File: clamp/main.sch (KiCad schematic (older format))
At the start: 36 parts, among them P1 CONN_01X12, U1 LM741, U2 LM741, U3 LM741, U4 LM741, U5 LM741, U6 LM741

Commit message: change to non hand-soldered 1206
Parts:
- C1, C10, C11, C12, C2, C3, C4, C5, C6, C7, C8, C9: footprint Capacitors_SMD:C_1206_HandSoldering -> Capacitors_SMD:C_1206
- R1, R10, R11, R12, R13, R2, R3, R4, R5, R6, R7, R8, R9: footprint Resistors_SMD:R_1206_HandSoldering -> Resistors_SMD:R_1206
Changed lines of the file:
@@
 F 0 "C3" H 7225 2050 50  0000 L CNN
 F 1 "C" H 7225 1850 50  0000 L CNN
-F 2 "Capacitors_SMD:C_1206_HandSoldering" H 7238 1800 50  0001 C CNN
+F 2 "Capacitors_SMD:C_1206" H 7238 1800 50  0001 C CNN
 F 3 "" H 7200 1950 50  0000 C CNN
 	1    7200 1950
@@
 F 0 "R7" V 5680 1500 50  0000 C CNN
 F 1 "R" V 5600 1500 50  0000 C CNN
-F 2 "Resistors_SMD:R_1206_HandSoldering" V 5530 1500 50  0001 C CNN
+F 2 "Resistors_SMD:R_1206" V 5530 1500 50  0001 C CNN
 F 3 "" H 5600 1500 50  0000 C CNN
 	1    5600 1500
@@
 F 0 "C5" H 7725 2050 50  0000 L CNN
 F 1 "C" H 7725 1850 50  0000 L CNN
-F 2 "Capacitors_SMD:C_1206_HandSoldering" H 7738 1800 50  0001 C CNN
+F 2 "Capacitors_SMD:C_1206" H 7738 1800 50  0001 C CNN
 F 3 "" H 7700 1950 50  0000 C CNN
 	1    7700 1950
@@
 F 0 "R2" V 2930 4000 50  0000 C CNN
 F 1 "R" V 2850 4000 50  0000 C CNN
-F 2 "Resistors_SMD:R_1206_HandSoldering" V 2780 4000 50  0001 C CNN
+F 2 "Resistors_SMD:R_1206" V 2780 4000 50  0001 C CNN
 F 3 "" H 2850 4000 50  0000 C CNN
 	1    2850 4000
@@
 F 0 "R1" V 2380 3450 50  0000 C CNN
 F 1 "R" V 2300 3450 50  0000 C CNN
-F 2 "Resistors_SMD:R_1206_HandSoldering" V 2230 3450 50  0001 C CNN
+F 2 "Resistors_SMD:R_1206" V 2230 3450 50  0001 C CNN
 F 3 "" H 2300 3450 50  0000 C CNN
 	1    2300 3450
@@
 F 0 "R3" V 3980 2050 50  0000 C CNN
 F 1 "R" V 3900 2050 50  0000 C CNN
-F 2 "Resistors_SMD:R_1206_HandSoldering" V 3830 2050 50  0001 C CNN
+F 2 "Resistors_SMD:R_1206" V 3830 2050 50  0001 C CNN
 F 3 "" H 3900 2050 50  0000 C CNN
 	1    3900 2050
@@
 F 0 "R4" V 3980 2250 50  0000 C CNN
 F 1 "R" V 3900 2250 50  0000 C CNN
-F 2 "Resistors_SMD:R_1206_HandSoldering" V 3830 2250 50  0001 C CNN
+F 2 "Resistors_SMD:R_1206" V 3830 2250 50  0001 C CNN
 F 3 "" H 3900 2250 50  0000 C CNN
 	1    3900 2250
@@
 F 0 "R6" V 4030 3350 50  0000 C CNN
 F 1 "R" V 3950 3350 50  0000 C CNN
-F 2 "Resistors_SMD:R_1206_HandSoldering" V 3880 3350 50  0001 C CNN
+F 2 "Resistors_SMD:R_1206" V 3880 3350 50  0001 C CNN
 F 3 "" H 3950 3350 50  0000 C CNN
 	1    3950 3350
@@
 F 0 "R5" V 4030 3100 50  0000 C CNN
 F 1 "R" V 3950 3100 50  0000 C CNN
-F 2 "Resistors_SMD:R_1206_HandSoldering" V 3880 3100 50  0001 C CNN
+F 2 "Resistors_SMD:R_1206" V 3880 3100 50  0001 C CNN
 F 3 "" H 3950 3100 50  0000 C CNN
 	1    3950 3100
@@
 F 0 "C2" H 7475 2050 50  0000 L CNN
 F 1 "C" H 7475 1850 50  0000 L CNN
-F 2 "Capacitors_SMD:C_1206_HandSoldering" H 7488 1800 50  0001 C CNN
+F 2 "Capacitors_SMD:C_1206" H 7488 1800 50  0001 C CNN
 F 3 "" H 7450 1950 50  0000 C CNN
 	1    7450 1950
@@
 F 0 "C1" H 7225 3300 50  0000 L CNN
 F 1 "C" H 7225 3100 50  0000 L CNN
-F 2 "Capacitors_SMD:C_1206_HandSoldering" H 7238 3050 50  0001 C CNN
+F 2 "Capacitors_SMD:C_1206" H 7238 3050 50  0001 C CNN
 F 3 "" H 7200 3200 50  0000 C CNN
 	1    7200 3200
@@
 F 0 "C6" H 7725 3300 50  0000 L CNN
 F 1 "C" H 7725 3100 50  0000 L CNN
-F 2 "Capacitors_SMD:C_1206_HandSoldering" H 7738 3050 50  0001 C CNN
+F 2 "Capacitors_SMD:C_1206" H 7738 3050 50  0001 C CNN
 F 3 "" H 7700 3200 50  0000 C CNN
 	1    7700 3200
@@
 F 0 "C4" H 7475 3300 50  0000 L CNN
 F 1 "C" H 7475 3100 50  0000 L CNN
-F 2 "Capacitors_SMD:C_1206_HandSoldering" H 7488 3050 50  0001 C CNN
+F 2 "Capacitors_SMD:C_1206" H 7488 3050 50  0001 C CNN
 F 3 "" H 7450 3200 50  0000 C CNN
 	1    7450 3200
@@
 F 0 "R9" V 2930 6600 50  0000 C CNN
 F 1 "R" V 2850 6600 50  0000 C CNN
-F 2 "Resistors_SMD:R_1206_HandSoldering" V 2780 6600 50  0001 C CNN
+F 2 "Resistors_SMD:R_1206" V 2780 6600 50  0001 C CNN
 F 3 "" H 2850 6600 50  0000 C CNN
 	1    2850 6600
@@
 F 0 "R8" V 2380 6050 50  0000 C CNN
 F 1 "R" V 2300 6050 50  0000 C CNN
-F 2 "Resistors_SMD:R_1206_HandSoldering" V 2230 6050 50  0001 C CNN
+F 2 "Resistors_SMD:R_1206" V 2230 6050 50  0001 C CNN
 F 3 "" H 2300 6050 50  0000 C CNN
 	1    2300 6050
@@
 F 0 "R10" V 3980 4650 50  0000 C CNN
 F 1 "R" V 3900 4650 50  0000 C CNN
-F 2 "Resistors_SMD:R_1206_HandSoldering" V 3830 4650 50  0001 C CNN
+F 2 "Resistors_SMD:R_1206" V 3830 4650 50  0001 C CNN
 F 3 "" H 3900 4650 50  0000 C CNN
 	1    3900 4650
@@
 F 0 "R11" V 3980 4850 50  0000 C CNN
 F 1 "R" V 3900 4850 50  0000 C CNN
-F 2 "Resistors_SMD:R_1206_HandSoldering" V 3830 4850 50  0001 C CNN
+F 2 "Resistors_SMD:R_1206" V 3830 4850 50  0001 C CNN
 F 3 "" H 3900 4850 50  0000 C CNN
 	1    3900 4850
@@
 F 0 "R13" V 4030 5950 50  0000 C CNN
 F 1 "R" V 3950 5950 50  0000 C CNN
-F 2 "Resistors_SMD:R_1206_HandSoldering" V 3880 5950 50  0001 C CNN
+F 2 "Resistors_SMD:R_1206" V 3880 5950 50  0001 C CNN
 F 3 "" H 3950 5950 50  0000 C CNN
 	1    3950 5950
@@
 F 0 "R12" V 4030 5700 50  0000 C CNN
 F 1 "R" V 3950 5700 50  0000 C CNN
-F 2 "Resistors_SMD:R_1206_HandSoldering" V 3880 5700 50  0001 C CNN
+F 2 "Resistors_SMD:R_1206" V 3880 5700 50  0001 C CNN
 F 3 "" H 3950 5700 50  0000 C CNN
 	1    3950 5700
@@
 F 0 "C7" H 7975 2050 50  0000 L CNN
 F 1 "C" H 7975 1850 50  0000 L CNN
-F 2 "Capacitors_SMD:C_1206_HandSoldering" H 7988 1800 50  0001 C CNN
+F 2 "Capacitors_SMD:C_1206" H 7988 1800 50  0001 C CNN
 F 3 "" H 7950 1950 50  0000 C CNN
 	1    7950 1950
@@
 F 0 "C11" H 8475 2050 50  0000 L CNN
 F 1 "C" H 8475 1850 50  0000 L CNN
-F 2 "Capacitors_SMD:C_1206_HandSoldering" H 8488 1800 50  0001 C CNN
+F 2 "Capacitors_SMD:C_1206" H 8488 1800 50  0001 C CNN
 F 3 "" H 8450 1950 50  0000 C CNN
 	1    8450 1950
@@
 F 0 "C9" H 8225 2050 50  0000 L CNN
 F 1 "C" H 8225 1850 50  0000 L CNN
-F 2 "Capacitors_SMD:C_1206_HandSoldering" H 8238 1800 50  0001 C CNN
+F 2 "Capacitors_SMD:C_1206" H 8238 1800 50  0001 C CNN
 F 3 "" H 8200 1950 50  0000 C CNN
 	1    8200 1950
@@
 F 0 "C8" H 7975 3300 50  0000 L CNN
 F 1 "C" H 7975 3100 50  0000 L CNN
-F 2 "Capacitors_SMD:C_1206_HandSoldering" H 7988 3050 50  0001 C CNN
+F 2 "Capacitors_SMD:C_1206" H 7988 3050 50  0001 C CNN
 F 3 "" H 7950 3200 50  0000 C CNN
 	1    7950 3200
@@
 F 0 "C12" H 8475 3300 50  0000 L CNN
 F 1 "C" H 8475 3100 50  0000 L CNN
-F 2 "Capacitors_SMD:C_1206_HandSoldering" H 8488 3050 50  0001 C CNN
+F 2 "Capacitors_SMD:C_1206" H 8488 3050 50  0001 C CNN
 F 3 "" H 8450 3200 50  0000 C CNN
 	1    8450 3200
@@
 F 0 "C10" H 8225 3300 50  0000 L CNN
 F 1 "C" H 8225 3100 50  0000 L CNN
-F 2 "Capacitors_SMD:C_1206_HandSoldering" H 8238 3050 50  0001 C CNN
+F 2 "Capacitors_SMD:C_1206" H 8238 3050 50  0001 C CNN
 F 3 "" H 8200 3200 50  0000 C CNN
 	1    8200 3200

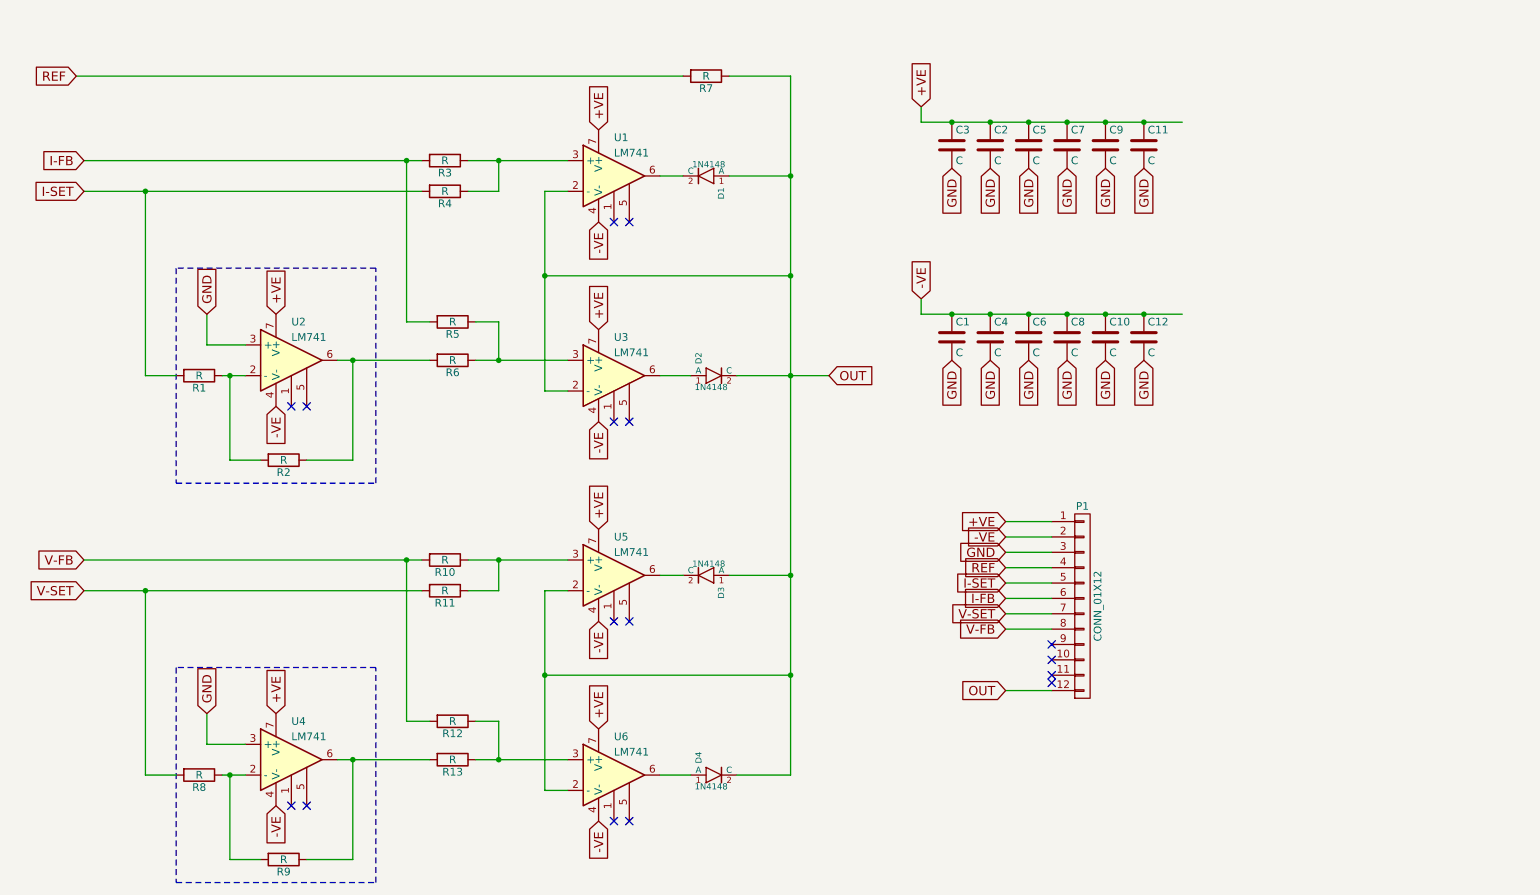
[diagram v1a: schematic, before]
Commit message: add 0R jumpers
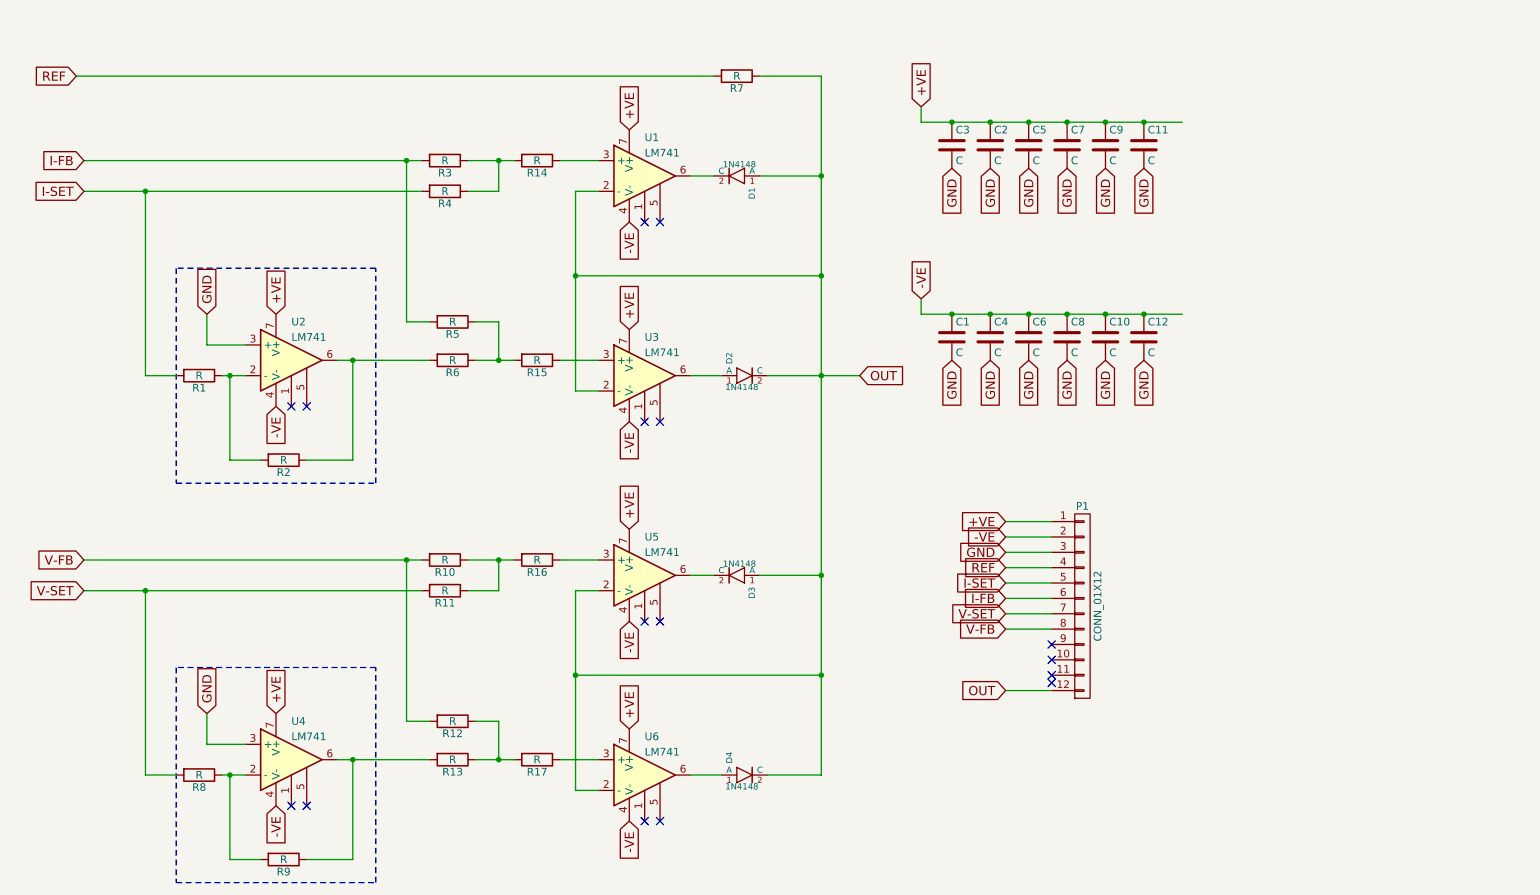
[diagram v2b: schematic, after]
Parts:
- added R14, R15, R16, R17: R, Resistors_SMD:R_1206, symbol R
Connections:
- net at R3.1, R4.1: now also R14.2; no longer U1.3 (+)
- net at R5.1, R6.1: now also R15.2; no longer U3.3 (+)
- net at R10.1, R11.1: now also R16.2; no longer U5.3 (+)
- net at R12.1, R13.1: now also R17.2; no longer U6.3 (+)
- new net: R14.1, U1.3 (+)
- new net: R15.1, U3.3 (+)
- new net: R16.1, U5.3 (+)
- new net: R17.1, U6.3 (+)
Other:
- moved on the sheet: D1, D2, D3, D4, R7, U1, U3, U5, U6

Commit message: add 0R values
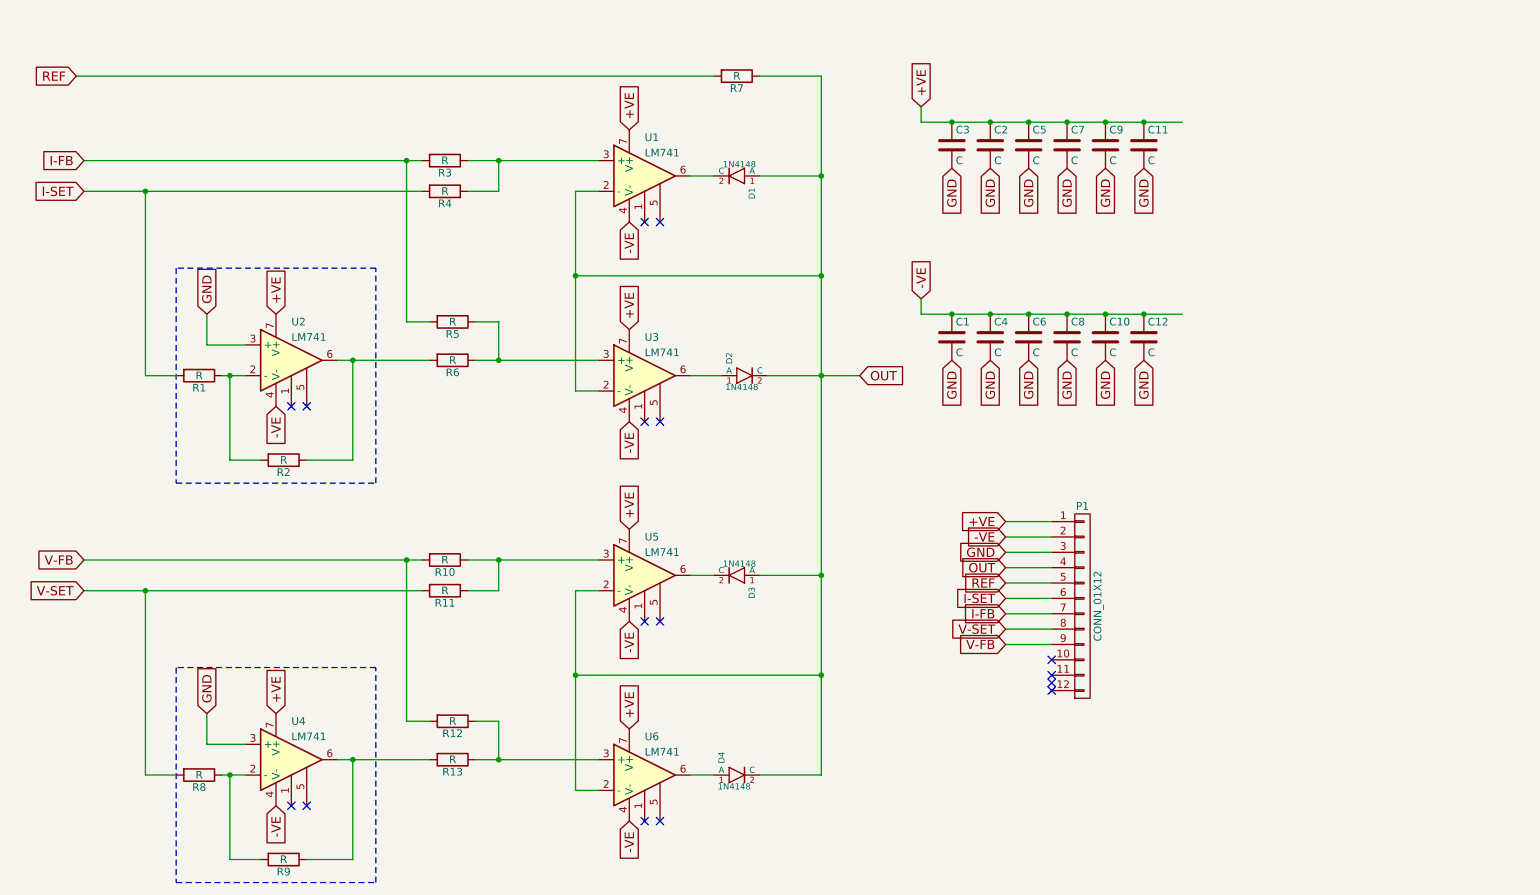
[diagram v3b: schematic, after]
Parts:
- removed R14, R15, R16, R17: R, Resistors_SMD:R_1206, symbol R
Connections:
- net I-FB: now also P1.7 (P7); no longer P1.6 (P6)
- net I-SET: now also P1.6 (P6); no longer P1.5 (P5)
- net OUT: now also P1.4 (P4); no longer P1.12 (P12)
- net REF: now also P1.5 (P5); no longer P1.4 (P4)
- net V-FB: now also P1.9 (P9); no longer P1.8 (P8)
- net V-SET: now also P1.8 (P8); no longer P1.7 (P7)
- net at U1.3 (+): now also R3.1, R4.1
- net at U3.3 (+): now also R5.1, R6.1
- net at U5.3 (+): now also R10.1, R11.1
- net at U6.3 (+): now also R12.1, R13.1
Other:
- moved on the sheet: D4
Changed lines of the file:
@@
 	4750 2250 4900 2250
 Wire Wire Line
-	4050 2050 4350 2050
+	4050 2050 4900 2050
 Wire Wire Line
 	5950 2150 6350 2150
@@
 	4250 3100 4250 3350
 Wire Wire Line
-	4100 3350 4350 3350
+	4100 3350 4900 3350
 Connection ~ 4250 3350
 Wire Notes Line
 	3450 4150 3450 2750
-Text GLabel 7550 4800 0    60   Input ~ 0
+Text GLabel 7550 4900 0    60   Input ~ 0
 I-SET
 Wire Wire Line
@@
 Text GLabel 7550 4600 0    60   Input ~ 0
 GND
-Text GLabel 7550 4700 0    60   Input ~ 0
+Text GLabel 7550 4800 0    60   Input ~ 0
 REF
 Wire Wire Line
@@
 	7850 4700 7550 4700
 Wire Wire Line
-	7850 4800 7550 4800
-Text GLabel 7550 4900 0    60   Input ~ 0
+	7850 4900 7550 4900
+Text GLabel 7550 5000 0    60   Input ~ 0
 I-FB
 Wire Wire Line
-	7850 4900 7550 4900
+	7850 5000 7550 5000
 Connection ~ 6350 3450
 Text GLabel 6600 3450 2    60   Input ~ 0
 OUT
-Text GLabel 7550 5500 0    60   Input ~ 0
+Text GLabel 7550 4700 0    60   Input ~ 0
 OUT
-Wire Wire Line
-	7850 5500 7550 5500
-NoConn ~ 7850 5200
 NoConn ~ 7850 5300
 NoConn ~ 7850 5450
@@
 	4750 4850 4900 4850
 Wire Wire Line
-	4050 4650 4350 4650
+	4050 4650 4900 4650
 Wire Wire Line
 	6350 4750 5950 4750
@@
 L 1N4148 D4
 U 1 1 580862BA
-P 5850 6050
-F 0 "D4" V 5775 6125 40  0000 L BNN
-F 1 "1N4148" H 5725 5975 40  0000 L CNN
-F 2 "Diodes_SMD:MiniMELF_Standard" H 5850 6200 30  0001 C CNN
-F 3 "" H 5850 6050 60  0000 C CNN
-	1    5850 6050
-	1    0    0    -1
-$EndComp
-Wire Wire Line
-	5500 6050 5700 6050
+P 5800 6050
+F 0 "D4" V 5725 6125 40  0000 L BNN
+F 1 "1N4148" H 5675 5975 40  0000 L CNN
+F 2 "Diodes_SMD:MiniMELF_Standard" H 5800 6200 30  0001 C CNN
+F 3 "" H 5800 6050 60  0000 C CNN
+	1    5800 6050
+	1    0    0    -1
+$EndComp
+Wire Wire Line
+	5500 6050 5650 6050
 Connection ~ 6350 5400
 $Comp
@@
 	4250 5700 4250 5950
 Wire Wire Line
-	4100 5950 4350 5950
+	4100 5950 4900 5950
 Connection ~ 4250 5950
 Wire Notes Line
@@
 Text GLabel 1550 4650 0    60   Input ~ 0
 V-FB
+Text GLabel 7550 5200 0    60   Input ~ 0
+V-FB
 Text GLabel 7550 5100 0    60   Input ~ 0
-V-FB
-Text GLabel 7550 5000 0    60   Input ~ 0
 V-SET
 $Comp
@@
 $EndComp
 Wire Wire Line
-	7550 5000 7850 5000
-Wire Wire Line
 	7550 5100 7850 5100
 Wire Wire Line
-	6350 6050 6000 6050
+	6350 6050 5950 6050
 $Comp
 L C C7
@@
 Text GLabel 8450 3350 3    60   Input ~ 0
 GND
-$Comp
-L R R14
-U 1 1 580AC25D
-P 4500 2050
-F 0 "R14" V 4580 2050 50  0000 C CNN
-F 1 "R" V 4500 2050 50  0000 C CNN
-F 2 "Resistors_SMD:R_1206" V 4430 2050 50  0001 C CNN
-F 3 "" H 4500 2050 50  0000 C CNN
-	1    4500 2050
-	0    1    1    0
-$EndComp
-$Comp
-L R R15
-U 1 1 580AC35A
-P 4500 3350
-F 0 "R15" V 4580 3350 50  0000 C CNN
-F 1 "R" V 4500 3350 50  0000 C CNN
-F 2 "Resistors_SMD:R_1206" V 4430 3350 50  0001 C CNN
-F 3 "" H 4500 3350 50  0000 C CNN
-	1    4500 3350
-	0    1    1    0
-$EndComp
-$Comp
-L R R16
-U 1 1 580AC44A
-P 4500 4650
-F 0 "R16" V 4580 4650 50  0000 C CNN
-F 1 "R" V 4500 4650 50  0000 C CNN
-F 2 "Resistors_SMD:R_1206" V 4430 4650 50  0001 C CNN
-F 3 "" H 4500 4650 50  0000 C CNN
-	1    4500 4650
-	0    1    1    0
-$EndComp
-$Comp
-L R R17
-U 1 1 580AC528
-P 4500 5950
-F 0 "R17" V 4580 5950 50  0000 C CNN
-F 1 "R" V 4500 5950 50  0000 C CNN
-F 2 "Resistors_SMD:R_1206" V 4430 5950 50  0001 C CNN
-F 3 "" H 4500 5950 50  0000 C CNN
-	1    4500 5950
-	0    1    1    0
-$EndComp
-Wire Wire Line
-	4650 2050 4900 2050
-Wire Wire Line
-	4650 3350 4900 3350
-Wire Wire Line
-	4650 4650 4900 4650
-Wire Wire Line
-	4650 5950 4900 5950
+Wire Wire Line
+	7550 4800 7850 4800
+Wire Wire Line
+	7850 5200 7550 5200
+NoConn ~ 7850 5500
 $EndSCHEMATC

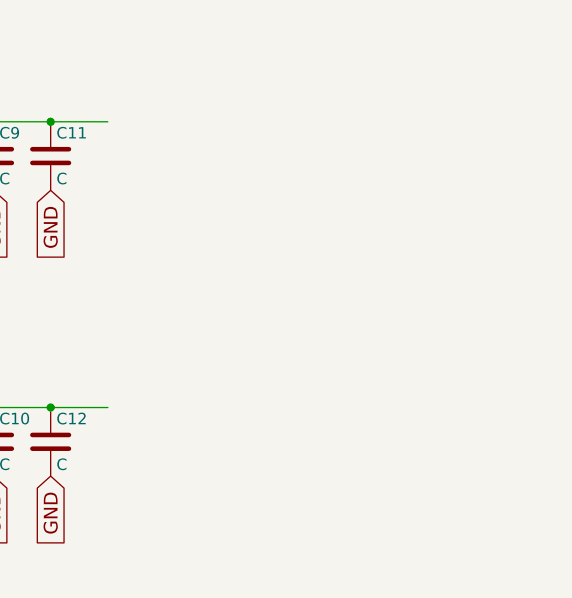
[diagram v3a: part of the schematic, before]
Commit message: added heirarchical sheet
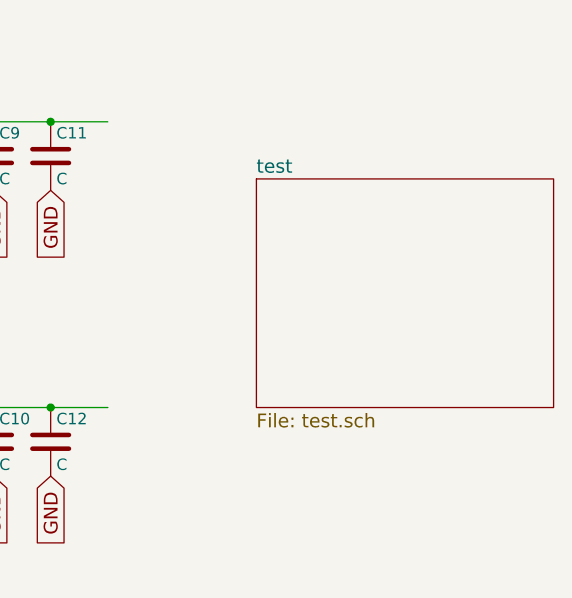
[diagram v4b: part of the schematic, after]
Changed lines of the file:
@@
 $Descr A4 11693 8268
 encoding utf-8
-Sheet 1 1
+Sheet 1 2
 Title ""
 Date ""
@@
 	7850 5200 7550 5200
 NoConn ~ 7850 5500
+$Sheet
+S 9350 2050 1300 1000
+U 580BA788
+F0 "test" 60
+F1 "test.sch" 60
+$EndSheet
 $EndSCHEMATC
